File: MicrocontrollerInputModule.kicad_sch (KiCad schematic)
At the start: 50 parts, among them J1 Conn_02x04_Odd_Even, J2 IPEX 20655-045E-01, U1 W25Q16JVUXIQ, U2 RP2040, U3 MCP23S17_ML, Y1 12.000MHz

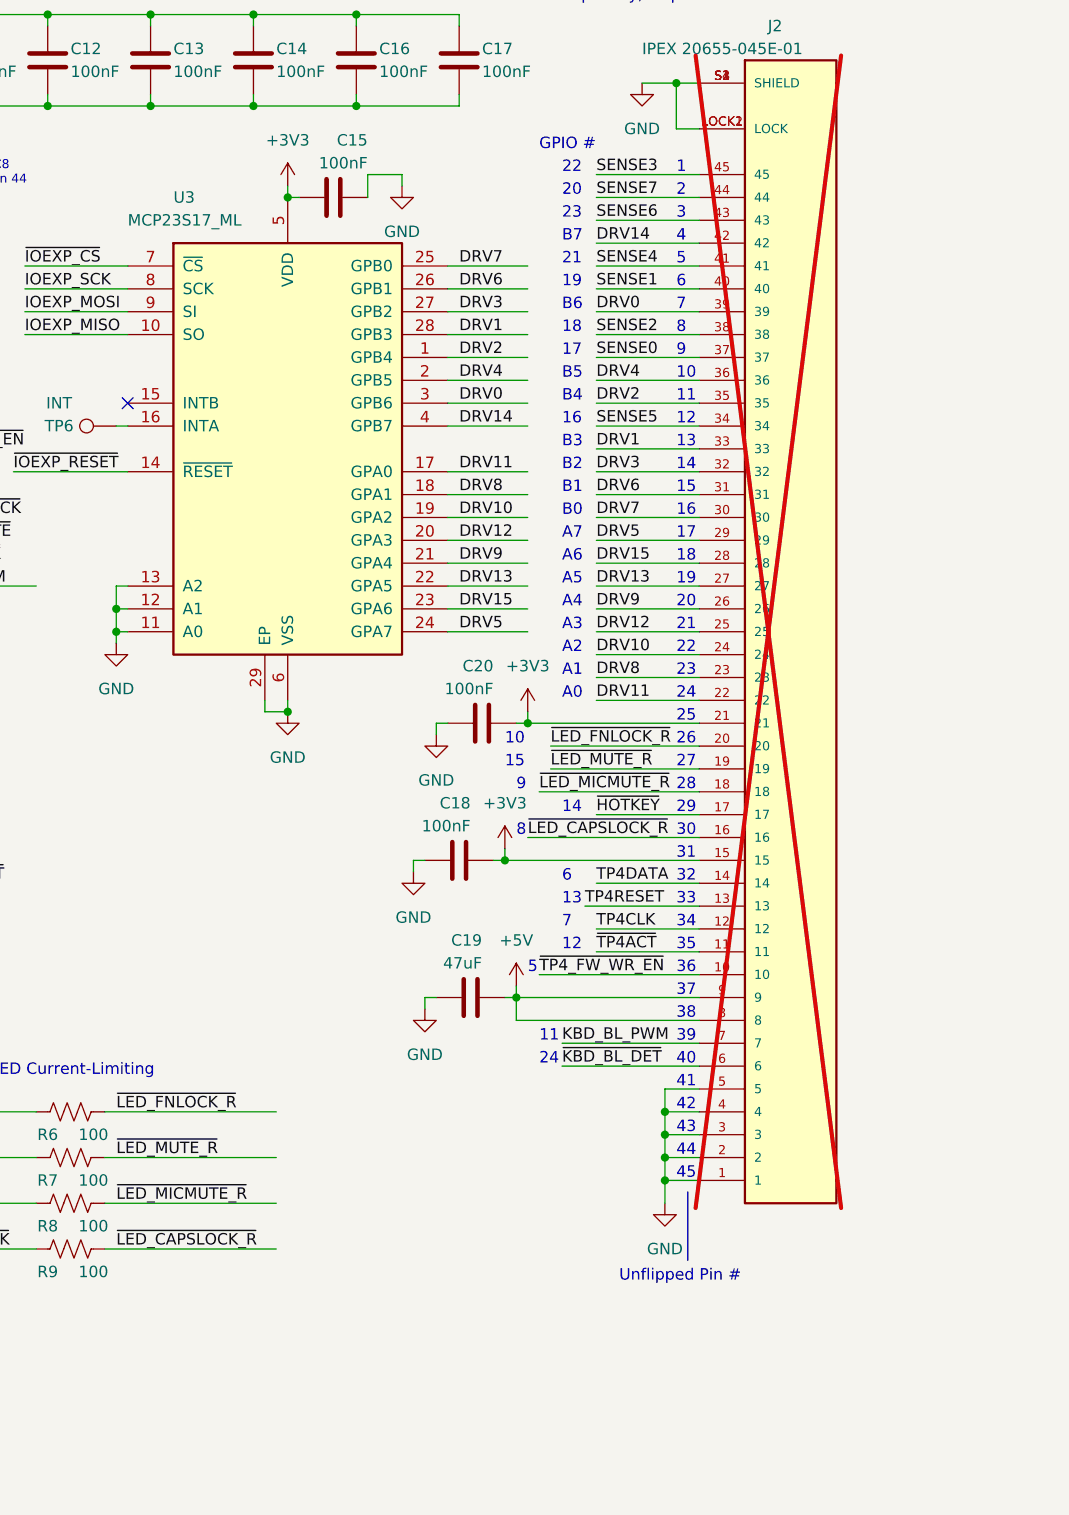
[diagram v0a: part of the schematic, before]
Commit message: Size test for relocating the FPC connector
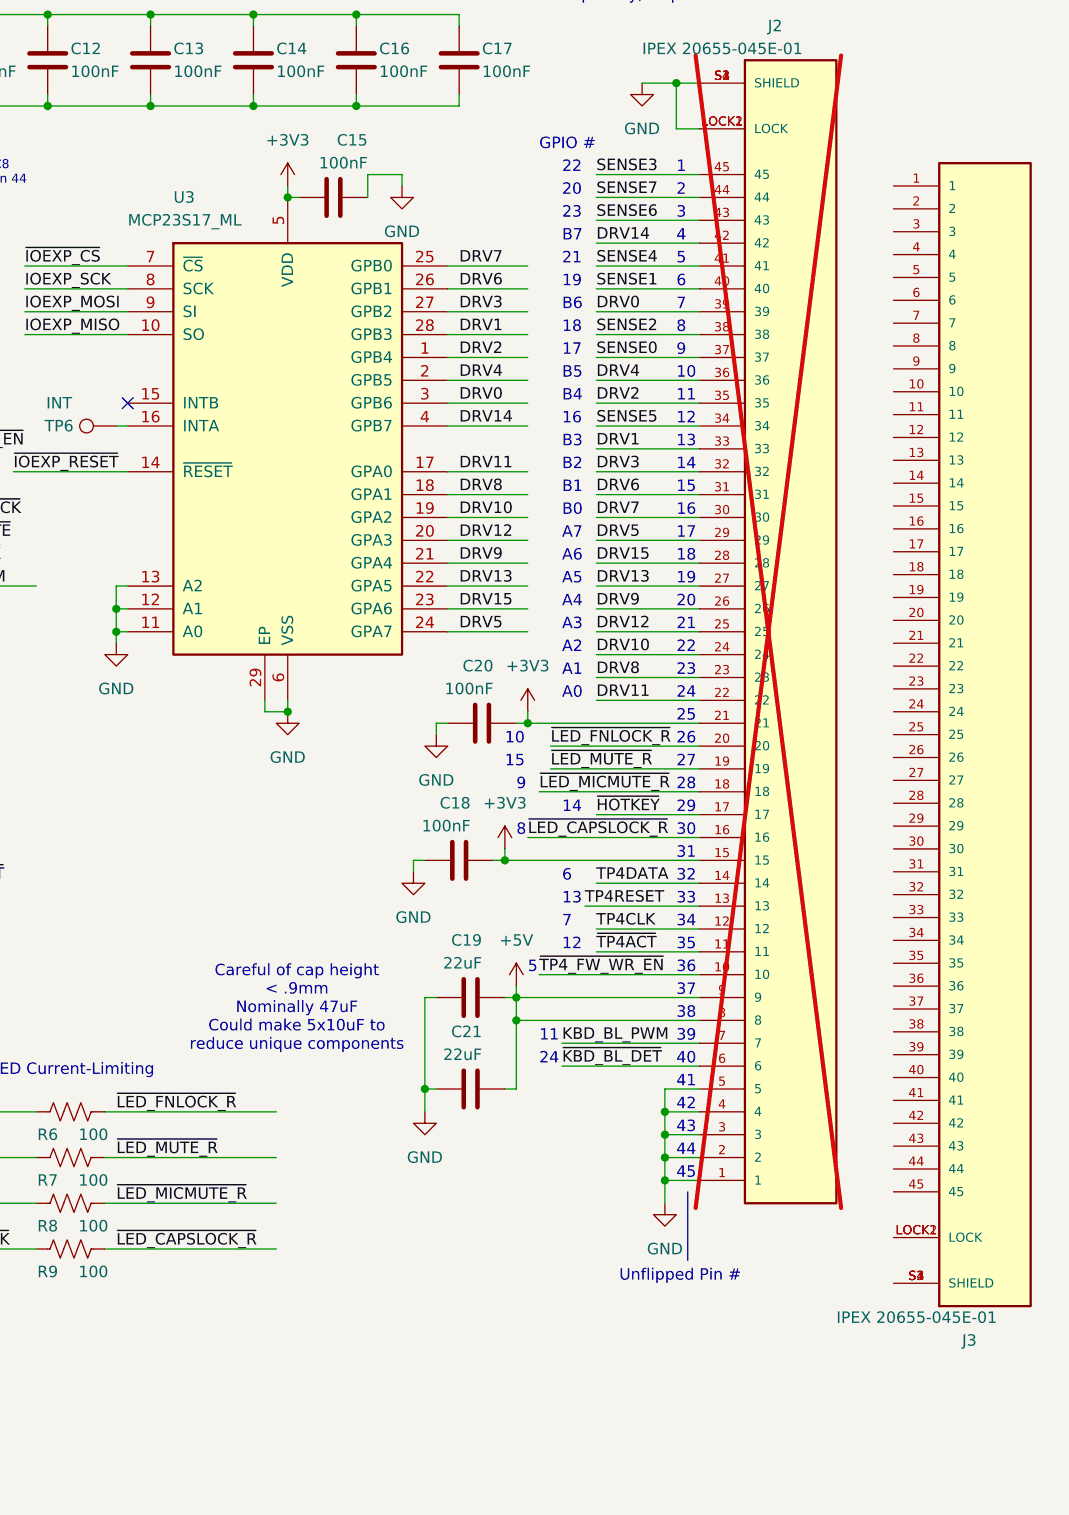
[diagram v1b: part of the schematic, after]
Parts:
- added C21: 22uF, Capacitor_SMD:C_0805_2012Metric, symbol Device:C
- added J3: IPEX 20655-045E-01, 20655-045E-01:0.3K-HX-45PWB, symbol 20655-045E-01:20655-045E-01
- C19: value 47uF -> 22uF
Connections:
- net +5V: now also C21.2
- net GND: now also C21.1
- new net: J3.LOCK1 (LOCK), J3.LOCK2 (LOCK)
- new net: J3.S1 (SHIELD), J3.S2 (SHIELD), J3.S3 (SHIELD), J3.S4 (SHIELD)
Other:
- note added: "Careful of cap height < .9mm Nominally 47uF Could make 5x10uF to reduce unique components"

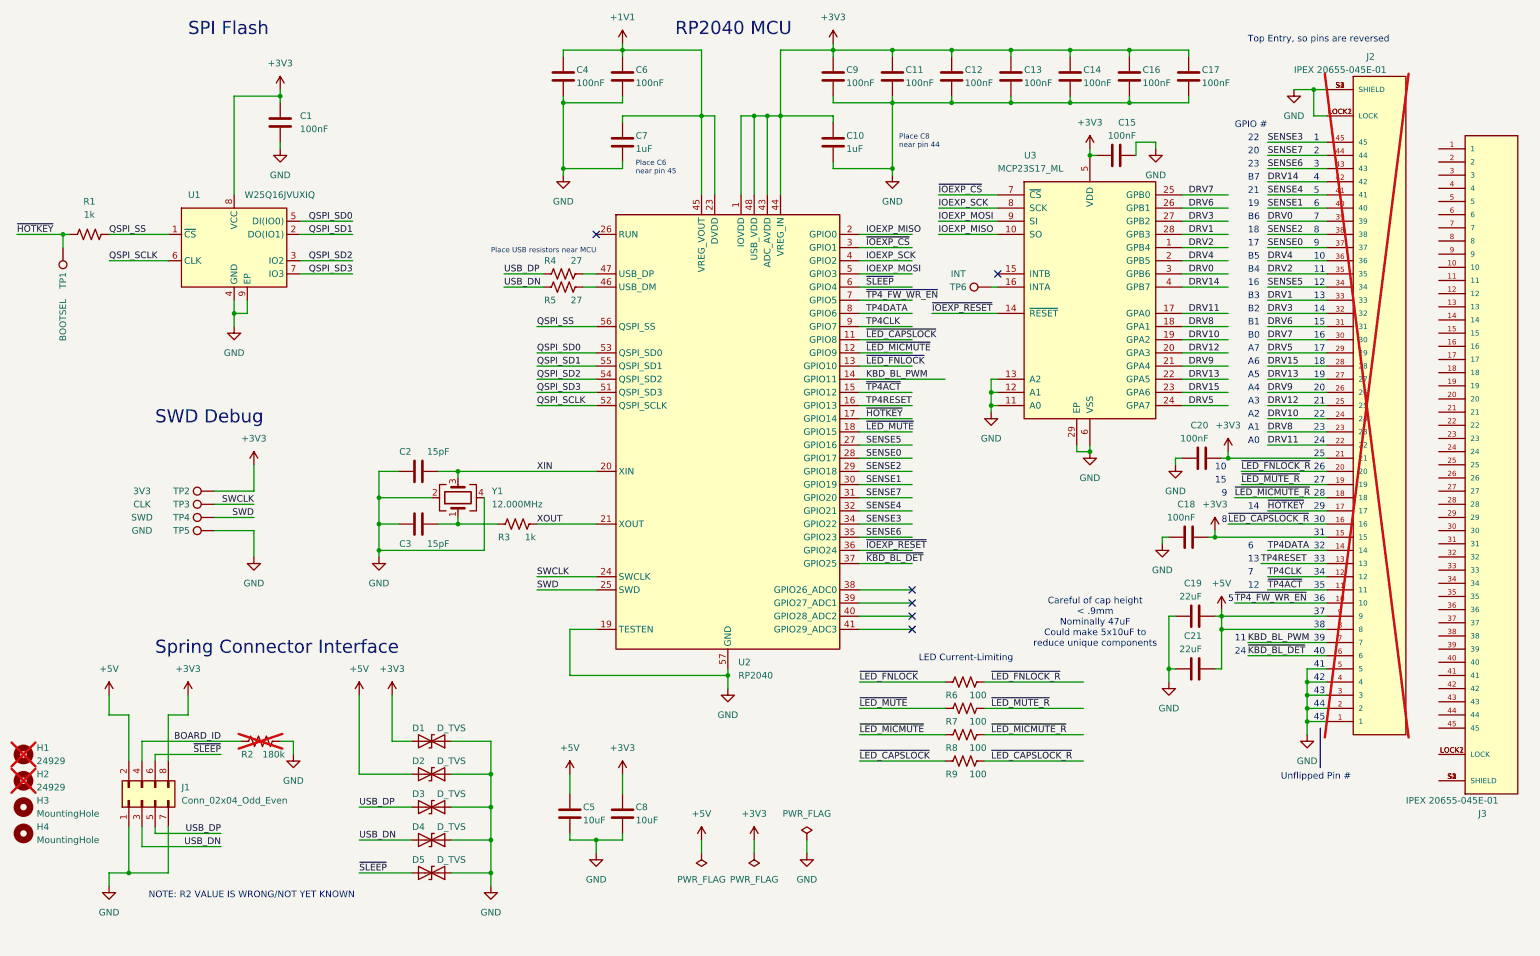
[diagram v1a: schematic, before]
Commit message: Update to use new FPC connector and position, fix sense resistor, etc
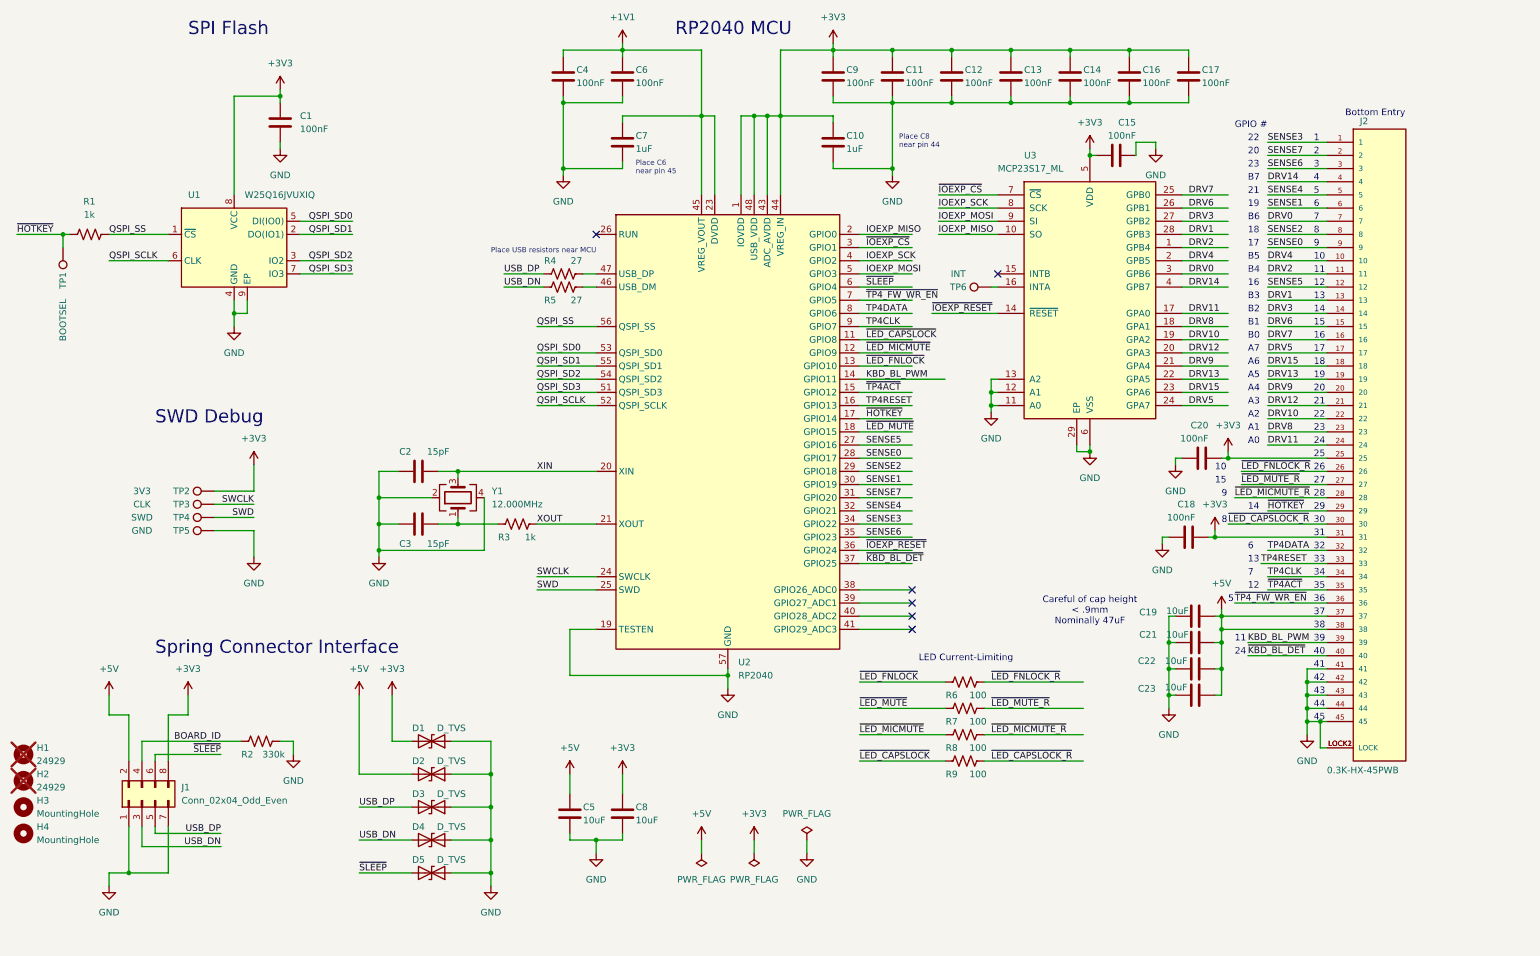
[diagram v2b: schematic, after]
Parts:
- removed J2: IPEX 20655-045E-01, 20655-045E-01:IPEX_20655-045E-01, symbol 20655-045E-01:20655-045E-01
- removed J3: IPEX 20655-045E-01, 20655-045E-01:0.3K-HX-45PWB, symbol 20655-045E-01:20655-045E-01
- added C22, C23: 10uF, Capacitor_SMD:C_0603_1608Metric, symbol Device:C
- added J2: 0.3K-HX-45PWB, 20655-045E-01:0.3K-HX-45PWB, symbol 20655-045E-01:0.3K-HX-45PWB
- C19, C21: value 22uF -> 10uF; footprint Capacitor_SMD:C_0805_2012Metric -> Capacitor_SMD:C_0603_1608Metric; Digikey 1276-1852-1-ND -> 1276-1869-1-ND; LCSC C16780 -> C96446; MP CL21A476MQYNNNE -> CL10A106MA8NRNC
- R2: value 180k -> 330k; footprint Resistor_SMD:R_0402_1005Metric -> Resistor_SMD:R_0603_1608Metric; LCSC (none) -> C23137; now fitted
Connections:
- net +3V3: now also J2.25, J2.31
- net +5V: now also C22.2, C23.2, J2.37, J2.38
- net DRV0: now also J2.7
- net DRV1: now also J2.13
- net DRV10: now also J2.22
- net DRV11: now also J2.24
- net DRV12: now also J2.21
- net DRV13: now also J2.19
- net DRV14: now also J2.4
- net DRV15: now also J2.18
- net DRV2: now also J2.11
- net DRV3: now also J2.14
- net DRV4: now also J2.10
- net DRV5: now also J2.17
- net DRV6: now also J2.15
- net DRV7: now also J2.16
- net DRV8: now also J2.23
- net DRV9: now also J2.20
- net GND: now also C22.1, C23.1, J2.41, J2.42, J2.43, J2.44, J2.45, J2.LOCK1 (LOCK), J2.LOCK2 (LOCK)
- net KBD_BL_PWM: now also J2.39
- net SENSE0: now also J2.9
- net SENSE1: now also J2.6
- net SENSE2: now also J2.8
- net SENSE3: now also J2.1
- net SENSE4: now also J2.5
- net SENSE5: now also J2.12
- net SENSE6: now also J2.3
- net SENSE7: now also J2.2
- net TP4CLK: now also J2.34
- net TP4DATA: now also J2.32
- net TP4RESET: now also J2.33
- net ~{HOTKEY}: now also J2.29
- net ~{KBD_BL_DET}: now also J2.40
- net ~{LED_CAPSLOCK_R}: now also J2.30
- net ~{LED_FNLOCK_R}: now also J2.26
- net ~{LED_MICMUTE_R}: now also J2.28
- net ~{LED_MUTE_R}: now also J2.27
- net ~{TP4ACT}: now also J2.35
- net ~{TP4_FW_WR_EN}: now also J2.36
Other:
- note added: "Bottom Entry"
- note added: "Careful of cap height < .9mm Nominally 47uF"
- note removed: "Careful of cap height < .9mm Nominally 47uF Could make 5x10uF to reduce unique components"
- note removed: "NOTE: R2 VALUE IS WRONG/NOT YET KNOWN"
- note removed: "Top Entry, so pins are reversed"
- note removed: "Unflipped Pin #"

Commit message: Second version sent to JLCPCB
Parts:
- added H5, H6, H7, H8: Tooling Hole, 20655-045E-01:JLCPCB Tooling Hole, symbol Mechanical:MountingHole
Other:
- moved on the sheet: H1, H2, H3, H4

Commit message: Update 3d models
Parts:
- H1, H2: now fitted
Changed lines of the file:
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@@
 		(in_bom yes)
 		(on_board yes)
-		(dnp yes)
+		(dnp no)
 		(property "Reference" "H1"
 			(at 19.05 154.94 0)
@@
 		(in_bom yes)
 		(on_board yes)
-		(dnp yes)
+		(dnp no)
 		(property "Reference" "H2"
 			(at 19.05 160.02 0)
